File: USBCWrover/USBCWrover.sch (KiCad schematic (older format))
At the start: 16 parts, among them J1 USB_C_Receptacle_USB2.0, J2 Conn_02x10_Odd_Even, J3 Conn_02x10_Odd_Even, SW2 SW_Push, U1 UMH3N, U2 CH340C, U3 HX9193-33GB, U4 ESP32-WROVER

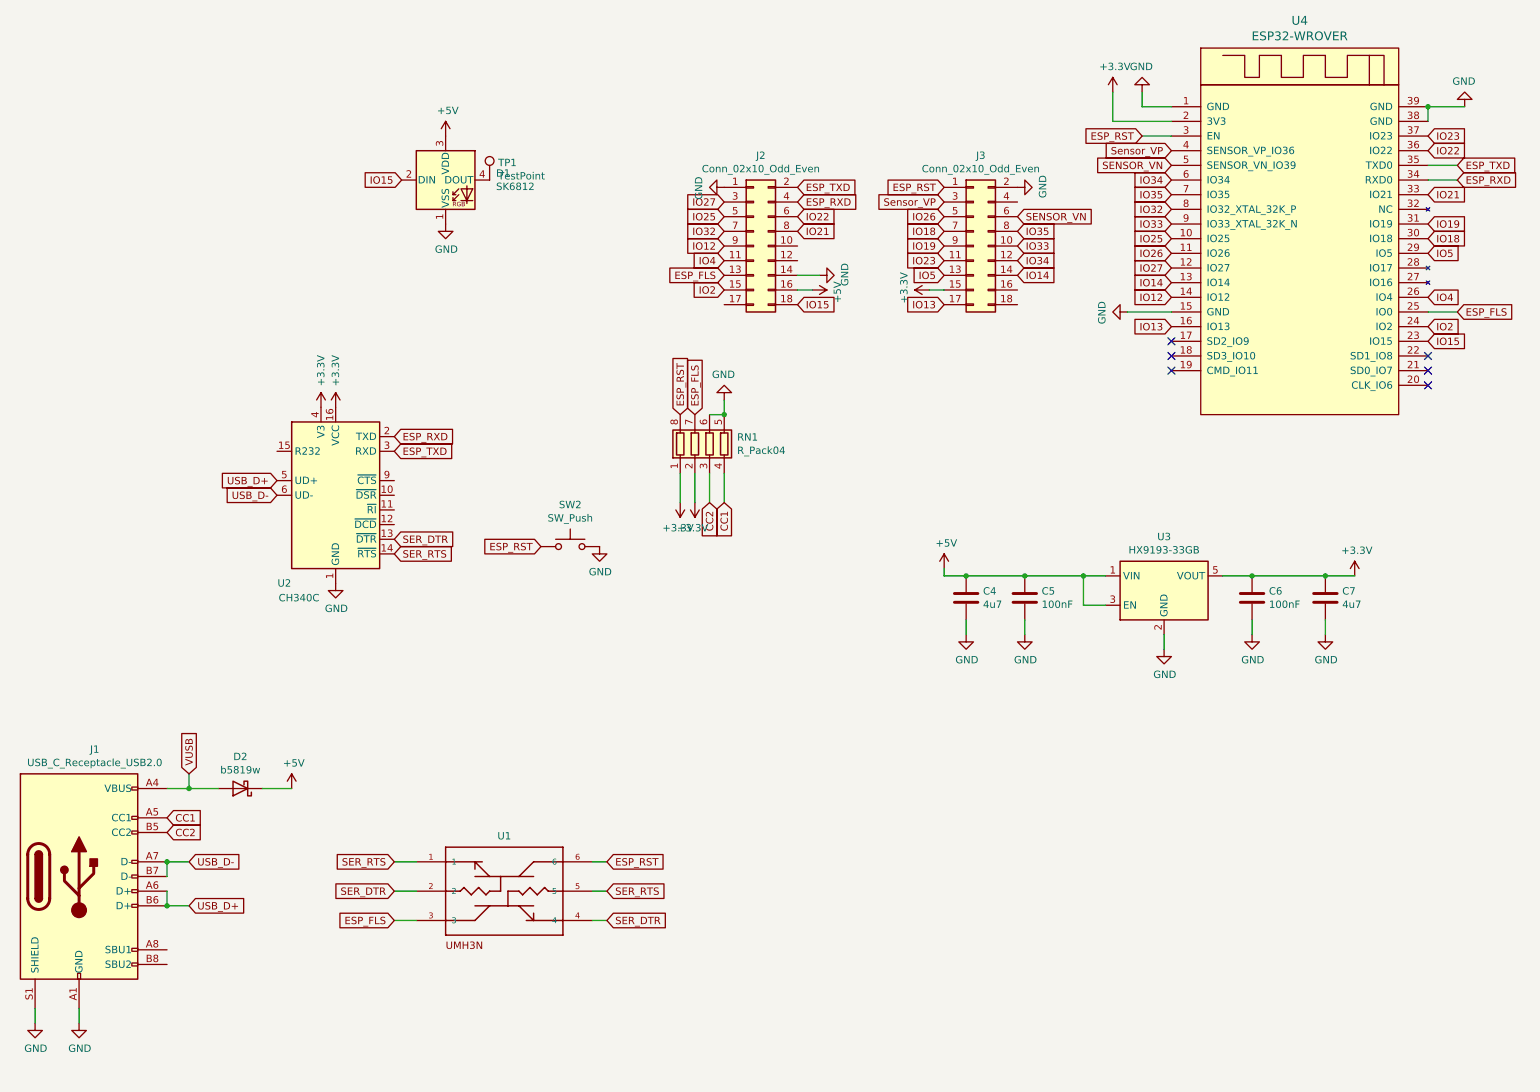
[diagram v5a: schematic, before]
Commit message: pads with text on top, resistor network instead of 4 resistors, usb serial rerouted
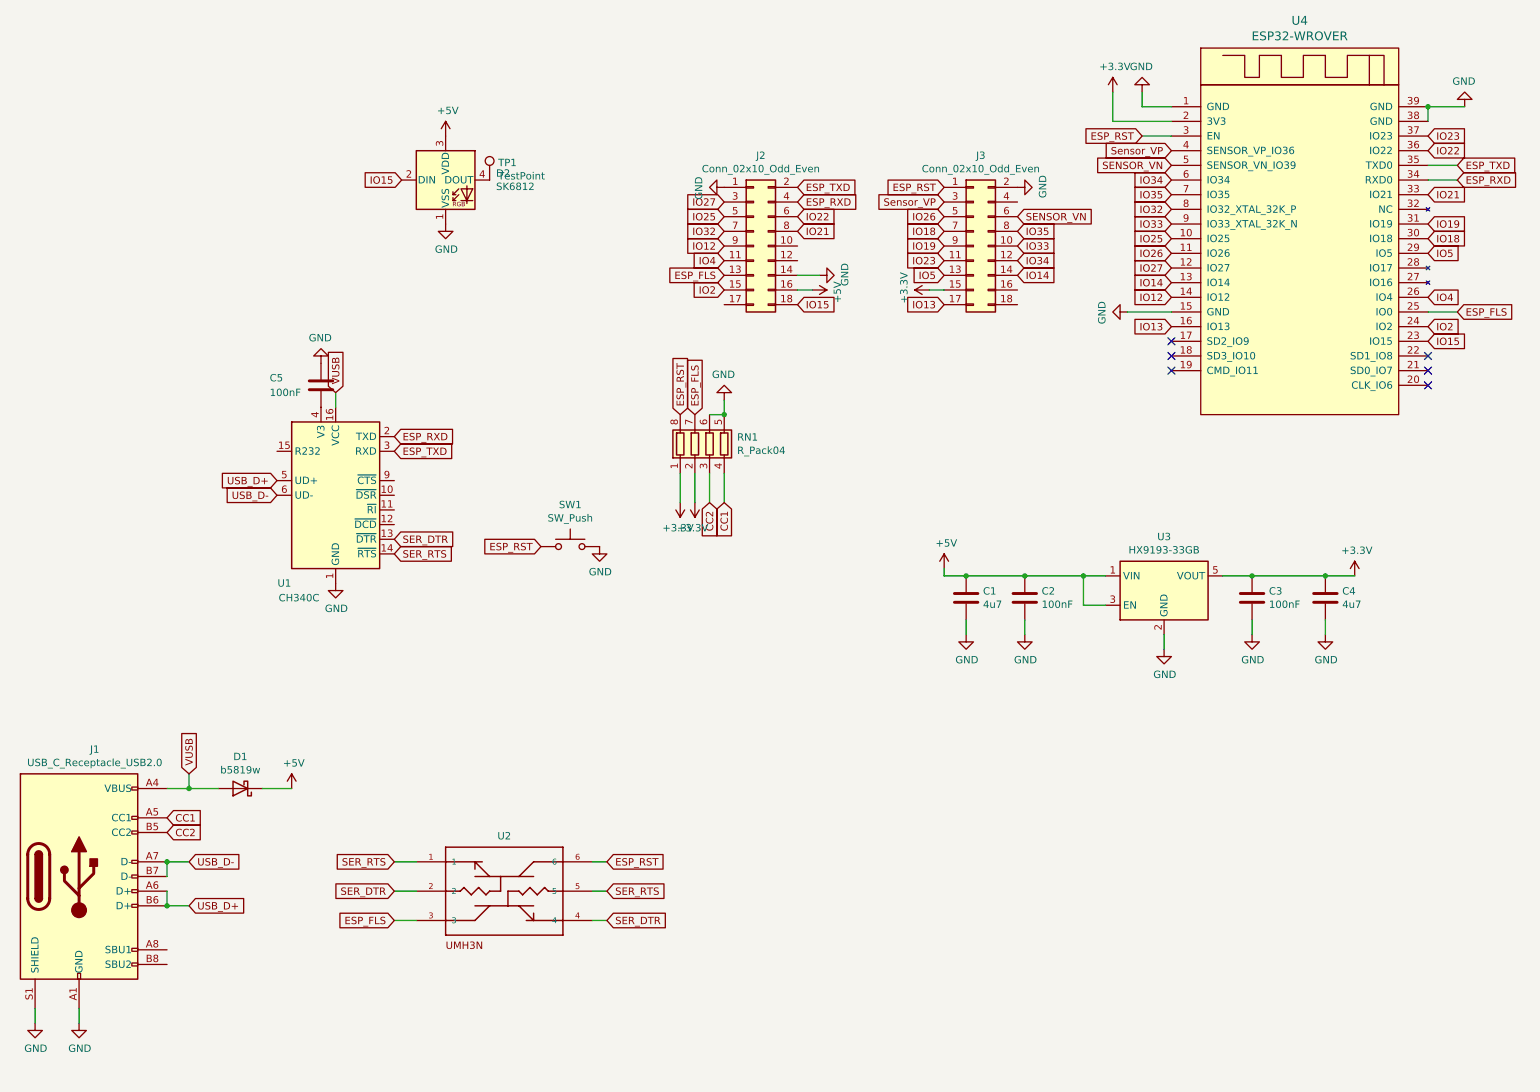
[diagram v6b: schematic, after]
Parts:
- added C5: 100nF, Capacitor_SMD:C_0805_2012Metric, symbol Device:C
- renumbered C4 to C1, C5 to C2, C6 to C3, C7 to C4, D2 to D1, D1 to D2, SW2 to SW1, U2 to U1, U1 to U2
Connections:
- net +3V3: no longer U1.16 (VCC), U1.4 (V3)
- net GND: now also C5.1
- net VUSB: now also U1.16 (VCC)
- new net: C5.2, U1.4 (V3)
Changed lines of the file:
@@
 	1100 7350 1100 7450
 $Comp
-L power:+5V #PWR021
+L power:+5V #PWR017
 U 1 1 5F42F75C
 P 7000 4350
-F 0 "#PWR021" H 7000 4200 50  0001 C CNN
+F 0 "#PWR017" H 7000 4200 50  0001 C CNN
 F 1 "+5V" H 7015 4523 50  0000 C CNN
 F 2 "" H 7000 4350 50  0001 C CNN
@@
 $EndComp
 $Comp
-L Device:C C5
+L Device:C C2
 U 1 1 5F4311CF
 P 7550 4550
-F 0 "C5" H 7665 4596 50  0000 L CNN
+F 0 "C2" H 7665 4596 50  0000 L CNN
 F 1 "100nF" H 7665 4505 50  0000 L CNN
 F 2 "Capacitor_SMD:C_0805_2012Metric" H 7588 4400 50  0001 C CNN
@@
 $EndComp
 $Comp
-L Device:C C4
+L Device:C C1
 U 1 1 5F432724
 P 7150 4550
-F 0 "C4" H 7265 4596 50  0000 L CNN
+F 0 "C1" H 7265 4596 50  0000 L CNN
 F 1 "4u7" H 7265 4505 50  0000 L CNN
 F 2 "Capacitor_SMD:C_0805_2012Metric" H 7188 4400 50  0001 C CNN
@@
 Connection ~ 7150 4400
 $Comp
-L Device:C C6
+L Device:C C3
 U 1 1 5F436356
 P 9100 4550
-F 0 "C6" H 9215 4596 50  0000 L CNN
+F 0 "C3" H 9215 4596 50  0000 L CNN
 F 1 "100nF" H 9215 4505 50  0000 L CNN
 F 2 "Capacitor_SMD:C_0805_2012Metric" H 9138 4400 50  0001 C CNN
@@
 $EndComp
 $Comp
-L Device:C C7
+L Device:C C4
 U 1 1 5F4367F1
 P 9600 4550
-F 0 "C7" H 9715 4596 50  0000 L CNN
+F 0 "C4" H 9715 4596 50  0000 L CNN
 F 1 "4u7" H 9715 4505 50  0000 L CNN
 F 2 "Capacitor_SMD:C_0805_2012Metric" H 9638 4400 50  0001 C CNN
@@
 Connection ~ 9600 4400
 $Comp
-L power:GND #PWR022
+L power:GND #PWR018
 U 1 1 5F439A51
 P 7150 4800
-F 0 "#PWR022" H 7150 4550 50  0001 C CNN
+F 0 "#PWR018" H 7150 4550 50  0001 C CNN
 F 1 "GND" H 7155 4627 50  0000 C CNN
 F 2 "" H 7150 4800 50  0001 C CNN
@@
 $EndComp
 $Comp
-L power:GND #PWR023
+L power:GND #PWR020
 U 1 1 5F439DED
 P 7550 4800
-F 0 "#PWR023" H 7550 4550 50  0001 C CNN
+F 0 "#PWR020" H 7550 4550 50  0001 C CNN
 F 1 "GND" H 7555 4627 50  0000 C CNN
 F 2 "" H 7550 4800 50  0001 C CNN
@@
 	8550 1400 8350 1400
 $Comp
-L power:+3.3V #PWR09
+L power:+3.3V #PWR021
 U 1 1 5F40675D
 P 8150 1100
-F 0 "#PWR09" H 8150 950 50  0001 C CNN
+F 0 "#PWR021" H 8150 950 50  0001 C CNN
 F 1 "+3.3V" H 8165 1273 50  0000 C CNN
 F 2 "" H 8150 1100 50  0001 C CNN
@@
 $EndComp
 $Comp
-L power:GND #PWR010
+L power:GND #PWR023
 U 1 1 5F4072FA
 P 8350 1100
-F 0 "#PWR010" H 8350 850 50  0001 C CNN
+F 0 "#PWR023" H 8350 850 50  0001 C CNN
 F 1 "GND" H 8355 927 50  0000 C CNN
 F 2 "" H 8350 1100 50  0001 C CNN
@@
 	8150 1300 8550 1300
 $Comp
-L power:GND #PWR012
+L power:GND #PWR028
 U 1 1 5F40B031
 P 10550 1200
-F 0 "#PWR012" H 10550 950 50  0001 C CNN
+F 0 "#PWR028" H 10550 950 50  0001 C CNN
 F 1 "GND" H 10555 1027 50  0000 C CNN
 F 2 "" H 10550 1200 50  0001 C CNN
@@
 ESP_TXD
 $Comp
-L power:GND #PWR013
+L power:GND #PWR012
 U 1 1 5F42F768
 P 5500 1750
-F 0 "#PWR013" H 5500 1500 50  0001 C CNN
+F 0 "#PWR012" H 5500 1500 50  0001 C CNN
 F 1 "GND" H 5505 1577 50  0000 C CNN
 F 2 "" H 5500 1750 50  0001 C CNN
@@
 ESP_RST
 $Comp
-L power:GND #PWR0101
+L power:GND #PWR019
 U 1 1 5F43EBB7
 P 7500 1750
-F 0 "#PWR0101" H 7500 1500 50  0001 C CNN
+F 0 "#PWR019" H 7500 1500 50  0001 C CNN
 F 1 "GND" H 7505 1577 50  0000 C CNN
 F 2 "" H 7500 1750 50  0001 C CNN
@@
 $EndComp
 $Comp
-L UMH3N:UMH3N U1
+L UMH3N:UMH3N U2
 U 1 1 5F3F176B
 P 4000 6550
-F 0 "U1" H 4000 6926 50  0000 C CNN
+F 0 "U2" H 4000 6926 50  0000 C CNN
 F 1 "UMH3N" H 4000 6550 50  0001 L BNN
 F 2 "Package_SO:TSOP-6_1.65x3.05mm_P0.95mm" H 4000 6550 50  0001 L BNN
@@
 IO12
 $Comp
-L power:GND #PWR0102
+L power:GND #PWR022
 U 1 1 5F42721B
 P 8250 2600
-F 0 "#PWR0102" H 8250 2350 50  0001 C CNN
+F 0 "#PWR022" H 8250 2350 50  0001 C CNN
 F 1 "GND" H 8255 2427 50  0000 C CNN
 F 2 "" H 8250 2600 50  0001 C CNN
@@
 IO5
 $Comp
-L power:+3.3V #PWR0103
+L power:+3.3V #PWR016
 U 1 1 5F42F069
 P 6900 2450
-F 0 "#PWR0103" H 6900 2300 50  0001 C CNN
+F 0 "#PWR016" H 6900 2300 50  0001 C CNN
 F 1 "+3.3V" H 6915 2623 50  0000 C CNN
 F 2 "" H 6900 2450 50  0001 C CNN
@@
 ESP_FLS
 $Comp
-L power:GND #PWR0104
+L power:GND #PWR015
 U 1 1 5F431C0D
 P 6150 2350
-F 0 "#PWR0104" H 6150 2100 50  0001 C CNN
+F 0 "#PWR015" H 6150 2100 50  0001 C CNN
 F 1 "GND" H 6155 2177 50  0000 C CNN
 F 2 "" H 6150 2350 50  0001 C CNN
@@
 IO2
 $Comp
-L power:+5V #PWR0105
+L power:+5V #PWR014
 U 1 1 5F433D70
 P 6100 2450
-F 0 "#PWR0105" H 6100 2300 50  0001 C CNN
+F 0 "#PWR014" H 6100 2300 50  0001 C CNN
 F 1 "+5V" H 6115 2623 50  0000 C CNN
 F 2 "" H 6100 2450 50  0001 C CNN
@@
 	8500 4800 8500 4900
 $Comp
-L LED:SK6812 D1
+L LED:SK6812 D2
 U 1 1 5F3F3DD8
 P 3600 1700
-F 0 "D1" H 3944 1746 50  0000 L CNN
+F 0 "D2" H 3944 1746 50  0000 L CNN
 F 1 "SK6812" H 3944 1655 50  0000 L CNN
 F 2 "LED_SMD:LED_SK6812_PLCC4_5.0x5.0mm_P3.2mm" H 3650 1400 50  0001 L TNN
@@
 $EndComp
 $Comp
-L power:+5V #PWR018
+L power:+5V #PWR07
 U 1 1 5F3F4B3A
 P 3600 1400
-F 0 "#PWR018" H 3600 1250 50  0001 C CNN
+F 0 "#PWR07" H 3600 1250 50  0001 C CNN
 F 1 "+5V" H 3615 1573 50  0000 C CNN
 F 2 "" H 3600 1400 50  0001 C CNN
@@
 $EndComp
 $Comp
-L power:GND #PWR028
+L power:GND #PWR08
 U 1 1 5F3F589D
 P 3600 2000
-F 0 "#PWR028" H 3600 1750 50  0001 C CNN
+F 0 "#PWR08" H 3600 1750 50  0001 C CNN
 F 1 "GND" H 3605 1827 50  0000 C CNN
 F 2 "" H 3600 2000 50  0001 C CNN
@@
 $EndComp
 $Comp
-L Interface_USB:CH340C U2
+L Interface_USB:CH340C U1
 U 1 1 5F4B13A2
 P 2850 3850
-F 0 "U2" H 2500 3250 50  0000 C CNN
+F 0 "U1" H 2500 3250 50  0000 C CNN
 F 1 "CH340C" H 2600 3150 50  0000 C CNN
 F 2 "Package_SO:SOIC-16_3.9x9.9mm_P1.27mm" H 2900 3300 50  0001 L CNN
@@
 ESP_RXD
 $Comp
-L power:GND #PWR011
+L power:GND #PWR06
 U 1 1 5F4B2704
 P 2850 4450
-F 0 "#PWR011" H 2850 4200 50  0001 C CNN
+F 0 "#PWR06" H 2850 4200 50  0001 C CNN
 F 1 "GND" H 2855 4277 50  0000 C CNN
 F 2 "" H 2850 4450 50  0001 C CNN
@@
 $EndComp
 $Comp
-L Device:D_Schottky D2
+L Device:D_Schottky D1
 U 1 1 5F4B5D3A
 P 2200 5850
-F 0 "D2" H 2200 5633 50  0000 C CNN
+F 0 "D1" H 2200 5633 50  0000 C CNN
 F 1 "b5819w" H 2200 5724 50  0000 C CNN
 F 2 "Diode_SMD:D_SOD-123" H 2200 5850 50  0001 C CNN
@@
 	2050 5850 1850 5850
 Connection ~ 1850 5850
-$Comp
-L power:+3.3V #PWR07
-U 1 1 5F4BBD55
-P 2750 3250
-F 0 "#PWR07" H 2750 3100 50  0001 C CNN
-F 1 "+3.3V" V 2750 3500 50  0000 C CNN
-F 2 "" H 2750 3250 50  0001 C CNN
-F 3 "" H 2750 3250 50  0001 C CNN
-	1    2750 3250
-	1    0    0    -1
-$EndComp
-$Comp
-L power:+3.3V #PWR08
-U 1 1 5F4BC61A
-P 2850 3250
-F 0 "#PWR08" H 2850 3100 50  0001 C CNN
-F 1 "+3.3V" V 2850 3500 50  0000 C CNN
-F 2 "" H 2850 3250 50  0001 C CNN
-F 3 "" H 2850 3250 50  0001 C CNN
-	1    2850 3250
-	1    0    0    -1
-$EndComp
 $Comp
 L power:+5V #PWR03
@@
 CC2
 $Comp
-L power:+3.3V #PWR0106
+L power:+3.3V #PWR011
 U 1 1 5F4EF3FD
 P 5300 3900
-F 0 "#PWR0106" H 5300 3750 50  0001 C CNN
+F 0 "#PWR011" H 5300 3750 50  0001 C CNN
 F 1 "+3.3V" H 5315 4073 50  0000 C CNN
 F 2 "" H 5300 3900 50  0001 C CNN
@@
 $EndComp
 $Comp
-L power:GND #PWR0107
+L power:GND #PWR013
 U 1 1 5F4EF922
 P 5500 3200
-F 0 "#PWR0107" H 5500 2950 50  0001 C CNN
+F 0 "#PWR013" H 5500 2950 50  0001 C CNN
 F 1 "GND" H 5505 3027 50  0000 C CNN
 F 2 "" H 5500 3200 50  0001 C CNN
@@
 	5500 3700 5500 3900
 $Comp
-L power:+3.3V #PWR0108
+L power:+3.3V #PWR010
 U 1 1 5F507441
 P 5200 3900
-F 0 "#PWR0108" H 5200 3750 50  0001 C CNN
+F 0 "#PWR010" H 5200 3750 50  0001 C CNN
 F 1 "+3.3V" H 5215 4073 50  0000 C CNN
 F 2 "" H 5200 3900 50  0001 C CNN
@@
 $EndComp
 $Comp
-L Switch:SW_Push SW2
+L Switch:SW_Push SW1
 U 1 1 5F518D04
 P 4450 4200
-F 0 "SW2" H 4450 4485 50  0000 C CNN
+F 0 "SW1" H 4450 4485 50  0000 C CNN
 F 1 "SW_Push" H 4450 4394 50  0000 C CNN
 F 2 "Button_Switch_SMD:SW_Push_1P1T_NO_CK_KSC6xxJ" H 4450 4400 50  0001 C CNN
@@
 ESP_RST
 $Comp
-L power:GND #PWR0109
+L power:GND #PWR09
 U 1 1 5F51CA0C
 P 4650 4200
-F 0 "#PWR0109" H 4650 3950 50  0001 C CNN
+F 0 "#PWR09" H 4650 3950 50  0001 C CNN
 F 1 "GND" H 4655 4027 50  0000 C CNN
 F 2 "" H 4650 4200 50  0001 C CNN
@@
 	1    0    0    -1
 $EndComp
+Text GLabel 2850 3150 1    50   Input ~ 0
+VUSB
+Wire Wire Line
+	2850 3150 2850 3250
+$Comp
+L Device:C C5
+U 1 1 5F4CE174
+P 2750 3100
+F 0 "C5" H 2400 3150 50  0000 L CNN
+F 1 "100nF" H 2400 3050 50  0000 L CNN
+F 2 "Capacitor_SMD:C_0805_2012Metric" H 2788 2950 50  0001 C CNN
+F 3 "~" H 2750 3100 50  0001 C CNN
+	1    2750 3100
+	1    0    0    -1
+$EndComp
+$Comp
+L power:GND #PWR04
+U 1 1 5F4CF216
+P 2750 2950
+F 0 "#PWR04" H 2750 2700 50  0001 C CNN
+F 1 "GND" H 2755 2777 50  0000 C CNN
+F 2 "" H 2750 2950 50  0001 C CNN
+F 3 "" H 2750 2950 50  0001 C CNN
+	1    2750 2950
+	-1   0    0    1
+$EndComp
 $EndSCHEMATC

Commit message: redesign
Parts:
- removed TP1: TestPoint, TestPoint:TestPoint_Pad_1.0x1.0mm, symbol Connector:TestPoint
- added D3: LED, LED_SMD:LED_1206_3216Metric_ReverseMount_Hole1.8x2.4mm, symbol Device:LED
- added R1: R, Resistor_SMD:R_0805_2012Metric_Pad1.15x1.40mm_HandSolder, symbol Device:R
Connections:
- net GND: now also R1.1
- net IO15: now also D3.2 (A)
- net at D2.4 (DOUT): now also J2.17 (Pin_17)
- new net: D3.1 (K), R1.2
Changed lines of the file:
@@
 IO15
-$Comp
-L Connector:TestPoint TP1
-U 1 1 5F3FFC2D
-P 3900 1700
-F 0 "TP1" H 3958 1818 50  0000 L CNN
-F 1 "TestPoint" H 3958 1727 50  0000 L CNN
-F 2 "TestPoint:TestPoint_Pad_1.0x1.0mm" H 4100 1700 50  0001 C CNN
-F 3 "~" H 4100 1700 50  0001 C CNN
-	1    3900 1700
-	1    0    0    -1
-$EndComp
 $Comp
 L Interface_USB:CH340C U1
@@
 	-1   0    0    1
 $EndComp
+Wire Wire Line
+	3900 1700 4750 1700
+Wire Wire Line
+	4750 1700 4750 2550
+Wire Wire Line
+	4750 2550 5500 2550
+$Comp
+L Device:LED D3
+U 1 1 5F558CA0
+P 4550 1100
+F 0 "D3" H 4543 845 50  0000 C CNN
+F 1 "LED" H 4543 936 50  0000 C CNN
+F 2 "LED_SMD:LED_1206_3216Metric_ReverseMount_Hole1.8x2.4mm" H 4550 1100 50  0001 C CNN
+F 3 "~" H 4550 1100 50  0001 C CNN
+	1    4550 1100
+	-1   0    0    1
+$EndComp
+$Comp
+L Device:R R1
+U 1 1 5F559D1C
+P 4850 1100
+F 0 "R1" V 4643 1100 50  0000 C CNN
+F 1 "R" V 4734 1100 50  0000 C CNN
+F 2 "Resistor_SMD:R_0805_2012Metric_Pad1.15x1.40mm_HandSolder" V 4780 1100 50  0001 C CNN
+F 3 "~" H 4850 1100 50  0001 C CNN
+	1    4850 1100
+	0    1    1    0
+$EndComp
+Text GLabel 4400 1100 0    50   Input ~ 0
+IO15
+$Comp
+L power:GND #PWR05
+U 1 1 5F55AE01
+P 5000 1100
+F 0 "#PWR05" H 5000 850 50  0001 C CNN
+F 1 "GND" H 5005 927 50  0000 C CNN
+F 2 "" H 5000 1100 50  0001 C CNN
+F 3 "" H 5000 1100 50  0001 C CNN
+	1    5000 1100
+	1    0    0    -1
+$EndComp
 $EndSCHEMATC
